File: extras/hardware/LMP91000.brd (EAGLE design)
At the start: 20.3 x 17.8 mm, 10 parts

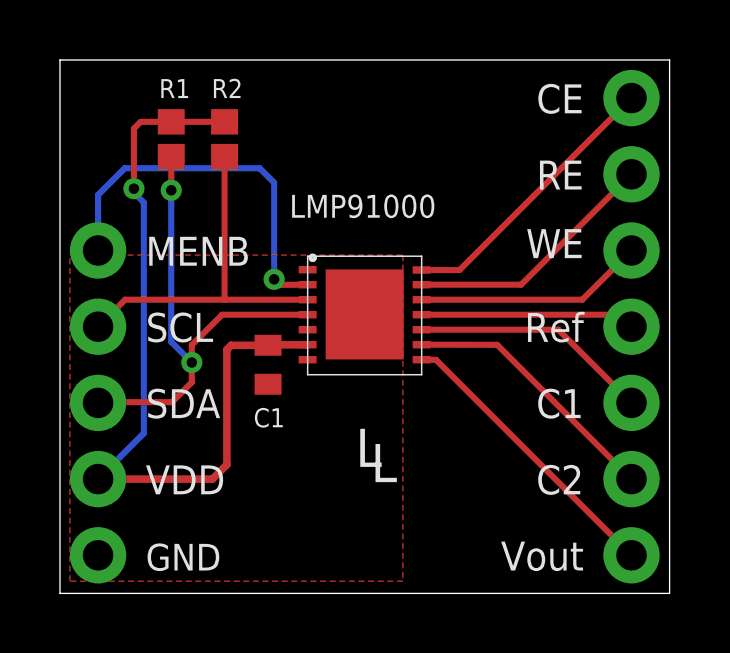
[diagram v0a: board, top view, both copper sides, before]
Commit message: Revert "Merge branch 'prototypes' of https://github.com/dzalf/LMP91000"
This reverts commit e035b5a0fbbc45ae6f48cbcd6f64b0519b6adfd6, reversing
changes made to 54f55630fa06b4778207c438d5379e7088d27feb.
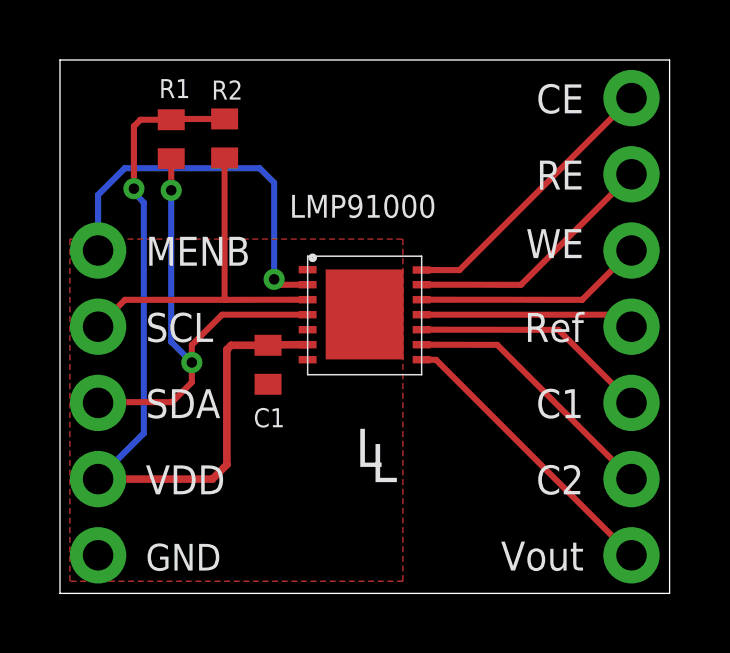
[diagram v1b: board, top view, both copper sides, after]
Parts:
- C1: device LinnesLab-Passives:C0402 -> CalvEngIO-Passives:C0402
- J1: device LinnesLab-Connectors:1X07_NO_SILK -> CalvEngIO-Connectors:1X07_NO_SILK
- J4: device LinnesLab-Connectors:1X05_NO_SILK -> CalvEngIO-Connectors:1X05_NO_SILK
- LMP91000: device LinnesLab-Sensors:WSON-14 -> CalvEngIO-Sensors:WSON-14
- LOGO1: device LinnesLab-Logos:OSHW-LOGO-S -> CalvEngIO-Logos:OSHW-LOGO-S
- R1, R2: device LinnesLab-Passives:R0402-BIGGER -> CalvEngIO-Passives:R0402
- U$1: device LinnesLab-Logos:LINNES.LAB.05 -> CalvEngIO-Logos:LINNES.LAB.05
- U$2: device LinnesLab-Logos:LINNES.LAB.LOGO -> CalvEngIO-Logos:LINNES.LAB.LOGO
- U$3: device LinnesLab-Logos:REV.B -> CalvEngIO-Symbols:REV.B
